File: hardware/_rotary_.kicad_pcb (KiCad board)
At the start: 2 copper layers, 40 x 80 mm, 18 parts, among them J1 mono_jack_3.5mm, J2 jst_xa_3, U1 TLV2372, U2 LM317

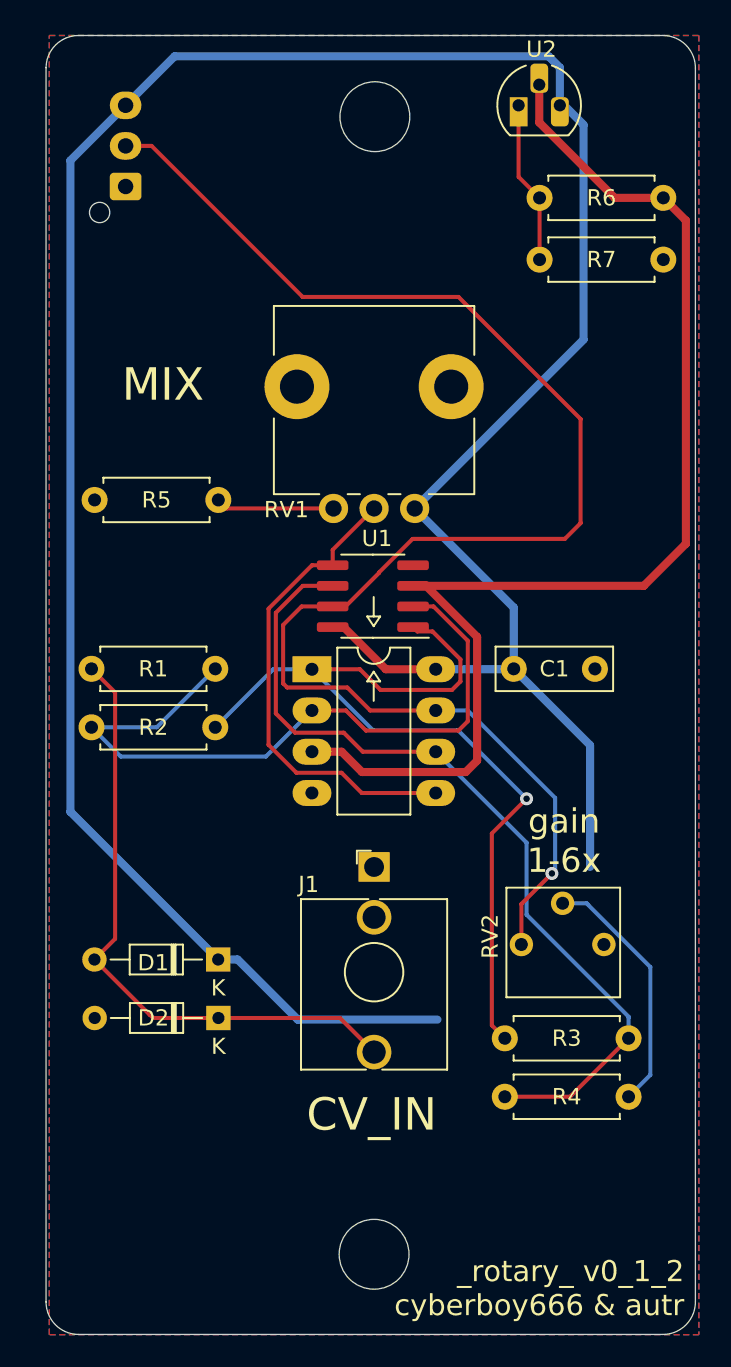
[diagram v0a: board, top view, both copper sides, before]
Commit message: updated circuit and panel to include envelope follower
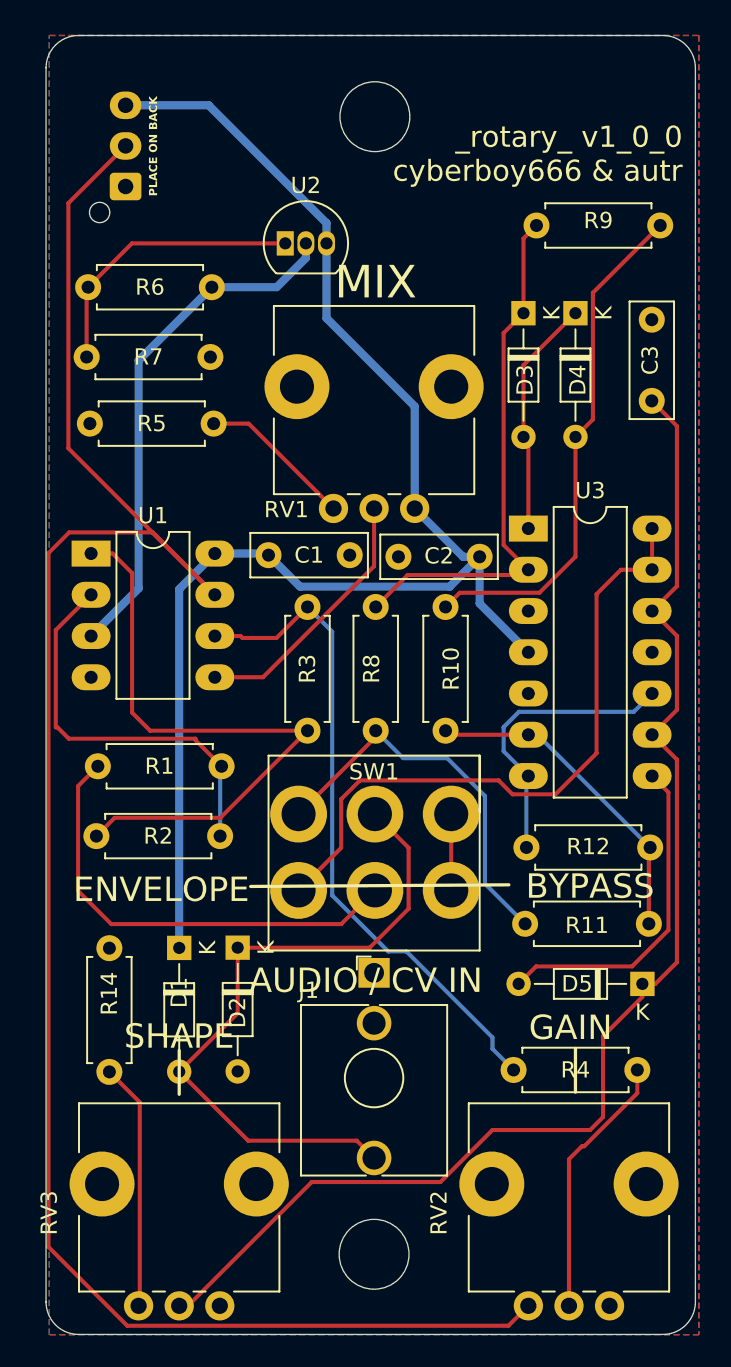
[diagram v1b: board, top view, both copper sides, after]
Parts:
- added C2: 0.1u, Capacitor_THT:C_Disc_D7.0mm_W2.5mm_P5.00mm, F.Cu at (101.5, 92.1)
- added C3: 1u, Capacitor_THT:C_Disc_D7.0mm_W2.5mm_P5.00mm, F.Cu at (117.1, 82.5)
- added D3: 1n4148, Diode_THT:D_DO-34_SOD68_P7.62mm_Horizontal, F.Cu at (109.2, 77.1)
- added D4: 1n4148, Diode_THT:D_DO-34_SOD68_P7.62mm_Horizontal, F.Cu at (112.4, 77.1)
- added D5: 1n4148, Diode_THT:D_DO-34_SOD68_P7.62mm_Horizontal, F.Cu at (116.5, 118.4)
- added R10: 10k, Resistor_THT:R_Axial_DIN0207_L6.3mm_D2.5mm_P7.62mm_Horizontal, F.Cu at (104.4, 95.2)
- added R11: 20k, Resistor_THT:R_Axial_DIN0207_L6.3mm_D2.5mm_P7.62mm_Horizontal, F.Cu at (109.3, 114.7)
- added R12: 20k, Resistor_THT:R_Axial_DIN0207_L6.3mm_D2.5mm_P7.62mm_Horizontal, F.Cu at (117.0, 110.0)
- added R14: 10k, Resistor_THT:R_Axial_DIN0207_L6.3mm_D2.5mm_P7.62mm_Horizontal, F.Cu at (83.7, 116.2)
- added R8: 10k, Resistor_THT:R_Axial_DIN0207_L6.3mm_D2.5mm_P7.62mm_Horizontal, F.Cu at (100.1, 102.8)
- added R9: 10k, Resistor_THT:R_Axial_DIN0207_L6.3mm_D2.5mm_P7.62mm_Horizontal, F.Cu at (110.0, 71.7)
- added RV3: 100k, lib_fp:Potentiometer_Vertical_Large, F.Cu at (90.5, 138.2)
- added SW1: SW_DPDT_x2, lib_fp:dpdt_mini_toggle_switch_tayda, F.Cu at (100.0, 100.8)
- added U3: TLV2374, Package_DIP:DIP-14_W7.62mm_LongPads, F.Cu at (109.5, 90.4)
- RV2: footprint lib_fp:tht_vertical_trim_3362 -> lib_fp:Potentiometer_Vertical_Large
- U1: footprint lib_fp:DIP-SOIC-8 -> Package_DIP:DIP-8_W7.62mm_LongPads
- U2: footprint Package_TO_SOT_THT:TO-92_HandSolder -> Package_TO_SOT_THT:TO-92_Inline
- moved R7 28.5 mm to (82.3, 79.8)
- moved R6 28.3 mm to (90.0, 75.5)
- moved R3 22.5 mm to (95.9, 102.8), turned to 90 degrees
- moved RV2 22.3 mm to (114.5, 138.2)
- moved U1 17.3 mm to (82.6, 91.9)
- moved U2 16.7 mm to (94.5, 72.8)
- moved C1 16.6 mm to (98.5, 92.0)
- moved R2 10.4 mm to (90.5, 109.3), turned to 180 degrees
- moved J1 6.52 mm to (100.0, 117.7)
- moved R1 6.01 mm to (83.0, 105.0)
- moved R5 4.71 mm to (90.1, 83.9)
- moved D2 4.49 mm to (91.6, 116.2), turned to -90 degrees
- moved D1 2.50 mm to (88.0, 116.2), turned to -90 degrees
- moved R4 1.74 mm to (108.6, 123.7)
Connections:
- D1 pad 2: Net-(D1-Pad2) -> Net-(D1-A)
- D2 pad 1: Net-(D1-Pad2) -> Net-(D1-A)
- J1 pad T: Net-(D1-Pad2) -> Net-(D1-A)
- R1 pad 1: Net-(D1-Pad2) -> Net-(SW1B-B)
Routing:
- net +5V: track 172.1 -> 90.7 mm
- net Net-(D5-K): track 0.00 -> 80.5 mm
- net +2.5V: track 75.5 -> 32.0 mm
- net Net-(D1-A): track 0.00 -> 41.5 mm
- net Net-(SW1B-A): track 0.00 -> 40.7 mm
- net Net-(D1-Pad2): track 38.6 -> 0.00 mm
- net Net-(D3-K): track 0.00 -> 33.0 mm
- net Net-(D4-A): track 0.00 -> 31.8 mm
- net Net-(SW1B-B): track 0.00 -> 28.2 mm
- net Net-(J2-Pin_2): track 95.5 -> 120.0 mm, vias 1 -> 0
- net Net-(SW1A-A): track 0.00 -> 24.4 mm
- net Net-(D5-A): track 0.00 -> 20.5 mm
- net Net-(U3B--): track 0.00 -> 20.3 mm
- net Net-(U1A--): track 44.2 -> 24.7 mm
- net Net-(U3C-+): track 0.00 -> 18.1 mm
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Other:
- board text added: "AUDIO / CV IN"
- board text added: "BYPASS"
- board text added: "ENVELOPE"
- board text added: "GAIN"
- board text added: "PLACE ON BACK"
- board text added: "SHAPE"
- board text added: "_rotary_ v1_0_0 cyberboy666 & autr"
- board text removed: "CV_IN"
- board text removed: "_rotary_ v0_1_2 cyberboy666 & autr"
- board text removed: "gain 1-6x"

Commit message: preparing v1_1_0 for release
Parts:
- removed REF** (x2): MountingHole_4.3mm_M4, MountingHole:MountingHole_4.3mm_M4
- added R13: 2.5k, Resistor_THT:R_Axial_DIN0207_L6.3mm_D2.5mm_P7.62mm_Horizontal, F.Cu at (116.5, 77.3)
- added R15: 1k, Resistor_THT:R_Axial_DIN0207_L6.3mm_D2.5mm_P7.62mm_Horizontal, F.Cu at (107.5, 71.7)
- RV2: value 5k_trim -> 5k_pot
- U2: footprint Package_TO_SOT_THT:TO-92_Inline -> Package_TO_SOT_THT:TO-92_HandSolder
- moved C3 14.4 mm to (117.4, 68.1), turned to 180 degrees
- moved R4 2.01 mm to (108.8, 121.7)
- moved D1 1.57 mm to (88.0, 114.6)
- moved D2 1.57 mm to (91.6, 114.6)
- moved R14 1.57 mm to (83.7, 114.6)
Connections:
- R11 pad 1: Net-(SW1A-A) -> Net-(SW1A-C)
- R8 pad 1: Net-(SW1A-A) -> Net-(SW1A-C)
- SW1 pad 4: Net-(SW1B-A) -> Net-(SW1A-A)
- SW1 pad 6: Net-(SW1A-C) -> Net-(SW1B-C)
- U3 pad 13: Net-(SW1B-A) -> Net-(U3D--)
- U3 pad 14: Net-(SW1B-A) -> Net-(SW1B-C)
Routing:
- net Net-(SW1B-C): track 0.00 -> 54.3 mm
- net Net-(SW1B-A): track 40.7 -> 0.00 mm
- net Net-(U3D--): track 0.00 -> 25.9 mm
- net Net-(SW1A-A): track 24.4 -> 4.70 mm
- net Net-(SW1A-C): track 4.70 -> 21.3 mm
- net Net-(D5-K): track 80.5 -> 94.9 mm
- net Net-(D1-A): track 41.5 -> 44.7 mm
- net Net-(R4-Pad2): track 17.0 -> 19.1 mm
- net +2.5V: track 32.0 -> 33.6 mm
- net Net-(R14-Pad2): track 15.2 -> 16.8 mm
- net Net-(U1B--): track 41.0 -> 39.9 mm
- net +5V: track 90.7 -> 89.7 mm
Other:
- board text added: "AUDIO CV IN"
- board text added: "_rotary_ v1_1_0 cyberboy666 & autr"
- board text removed: "AUDIO / CV IN"
- board text removed: "_rotary_ v1_0_0 cyberboy666 & autr"
